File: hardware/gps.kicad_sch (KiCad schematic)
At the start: 13 parts, among them U4 L96-M33

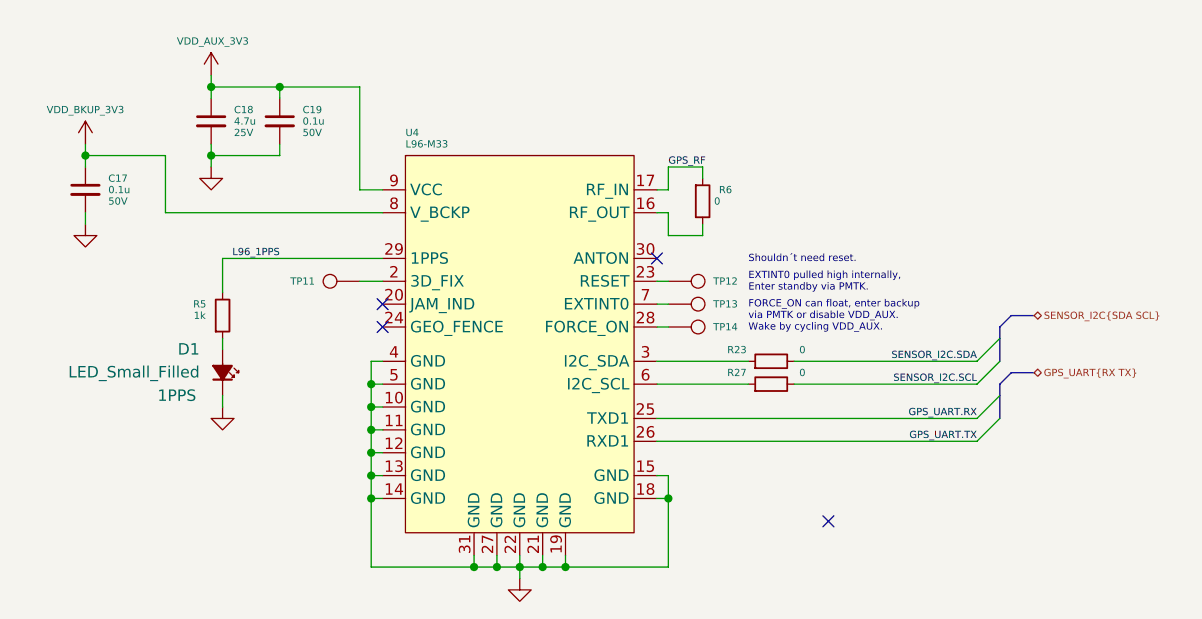
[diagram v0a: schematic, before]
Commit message: schematic tidy up, component placement, shielding investigation
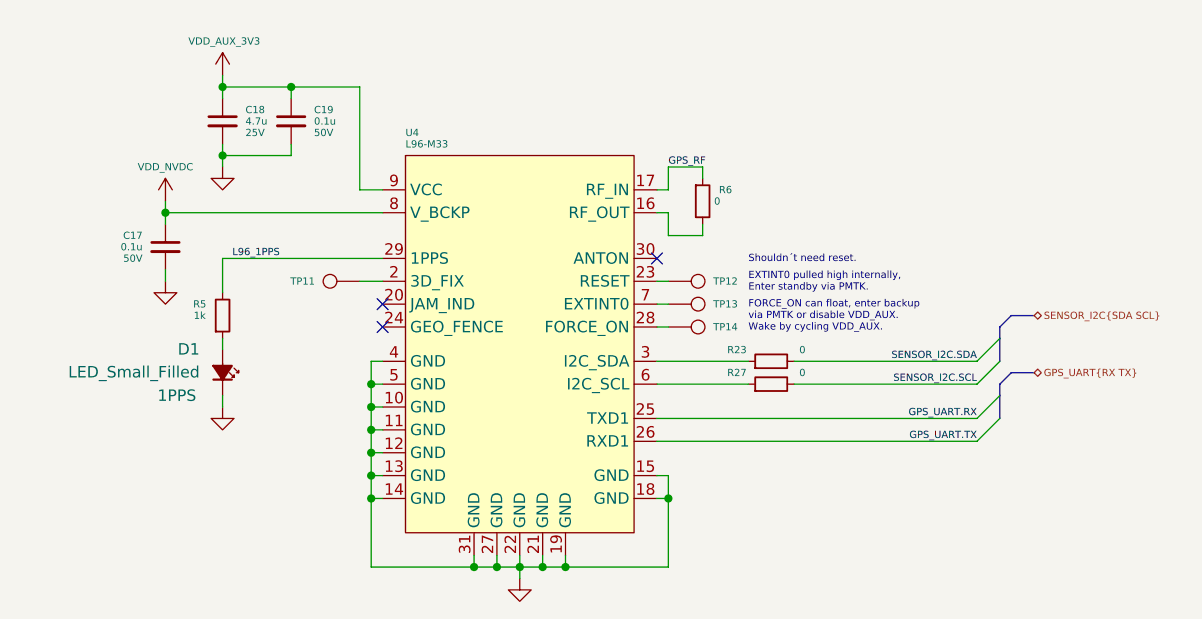
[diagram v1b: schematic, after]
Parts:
- TP12: value GPS_3DF -> GPS_RST
- TP13: value GPS_3DF -> GPS_INT
- TP14: value GPS_3DF -> GPS_FON
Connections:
- net VCC_BKUP_3V3 renamed VDD_NVDC
- no-connect marks 4 -> 3
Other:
- moved on the sheet: C17, C18, C19

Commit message: minor sch tweaks, more layout, added power emc shield
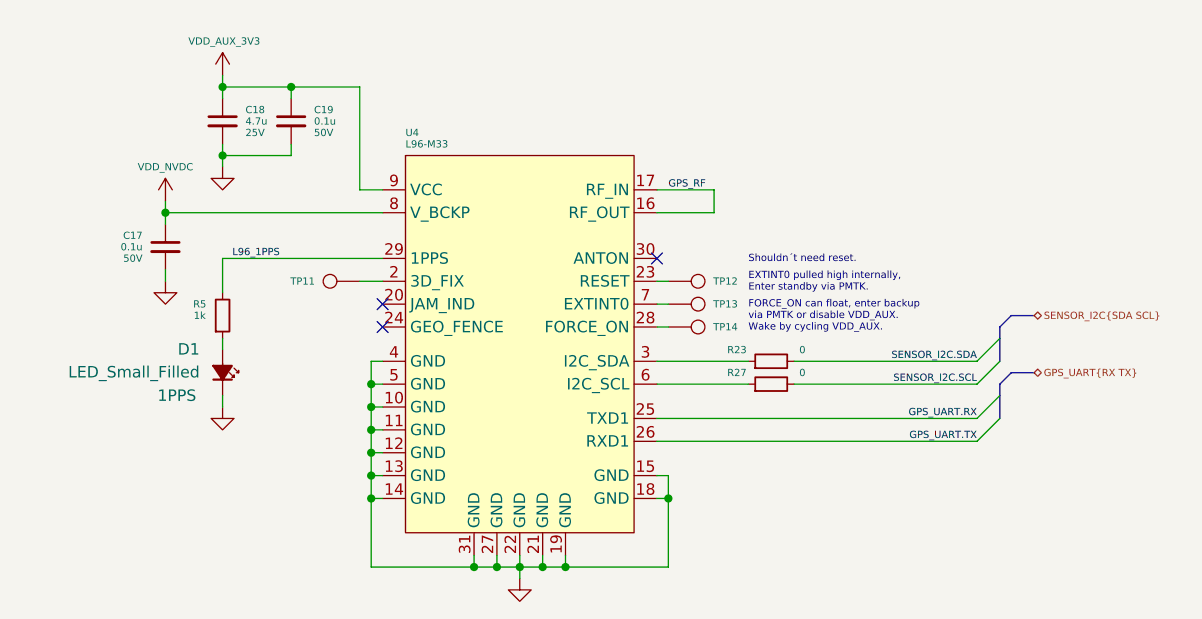
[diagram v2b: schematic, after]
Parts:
- removed R6: 0, Resistor_SMD:R_0402_1005Metric, symbol Device:R_Small
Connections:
- net GPS_RF: now also U4.16 (RF_OUT)
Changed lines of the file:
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@@
-    (stroke (width 0) (type default) (color 0 0 0 0))
-  )
-  (wire (pts (xy 168.91 85.09) (xy 172.72 85.09))
     (stroke (width 0) (type default) (color 0 0 0 0))
   )
@@
     (stroke (width 0) (type default) (color 0 0 0 0))
   )
-  (wire (pts (xy 172.72 85.09) (xy 172.72 83.82))
-    (stroke (width 0) (type default) (color 0 0 0 0))
-  )
   (wire (pts (xy 135.89 109.22) (xy 135.89 111.76))
     (stroke (width 0) (type default) (color 0 0 0 0))
@@
     (stroke (width 0) (type default) (color 0 0 0 0))
   )
-  (wire (pts (xy 168.91 80.01) (xy 168.91 77.47))
-    (stroke (width 0) (type default) (color 0 0 0 0))
-  )
   (wire (pts (xy 127 69.85) (xy 127 68.58))
     (stroke (width 0) (type default) (color 0 0 0 0))
@@
     (stroke (width 0) (type default) (color 0 0 0 0))
   )
-  (wire (pts (xy 167.64 80.01) (xy 168.91 80.01))
+  (wire (pts (xy 167.64 80.01) (xy 173.99 80.01))
     (stroke (width 0) (type default) (color 0 0 0 0))
   )
@@
     (stroke (width 0) (type default) (color 0 0 0 0))
   )
-  (wire (pts (xy 168.91 77.47) (xy 172.72 77.47))
-    (stroke (width 0) (type default) (color 0 0 0 0))
-  )
   (bus (pts (xy 205.74 101.6) (xy 207.01 100.33))
     (stroke (width 0) (type default) (color 0 0 0 0))
@@
     (stroke (width 0) (type default) (color 0 0 0 0))
   )
-  (wire (pts (xy 168.91 82.55) (xy 168.91 85.09))
+  (wire (pts (xy 173.99 80.01) (xy 173.99 82.55))
     (stroke (width 0) (type default) (color 0 0 0 0))
   )
@@
     (stroke (width 0) (type default) (color 0 0 0 0))
   )
-  (wire (pts (xy 167.64 82.55) (xy 168.91 82.55))
+  (wire (pts (xy 167.64 82.55) (xy 173.99 82.55))
     (stroke (width 0) (type default) (color 0 0 0 0))
   )
@@
   )
   (bus (pts (xy 205.74 95.25) (xy 205.74 96.52))
-    (stroke (width 0) (type default) (color 0 0 0 0))
-  )
-  (wire (pts (xy 172.72 77.47) (xy 172.72 78.74))
     (stroke (width 0) (type default) (color 0 0 0 0))
   )
@@
     (effects (font (size 0.8 0.8)) (justify right bottom))
   )
-  (label "GPS_RF" (at 168.91 77.47 0)
+  (label "GPS_RF" (at 168.91 80.01 0)
     (effects (font (size 0.8 0.8)) (justify left bottom))
   )
@@
     )
     (pin "1")
-    (pin "2")
-  )
-  (symbol (lib_id "Device:R_Small") (at 172.72 81.28 0) (unit 1)
-    (in_bom yes) (on_board yes)
-    (property "Reference" "R6" (id 0) (at 175.26 80.01 0)
-      (effects (font (size 0.8 0.8)))
-    )
-    (property "Value" "0" (id 1) (at 173.99 81.28 0)
-      (effects (font (size 0.8 0.8)) (justify left))
-    )
-    (property "Footprint" "Resistor_SMD:R_0402_1005Metric" (id 2) (at 172.72 81.28 0)
-      (effects (font (size 0.8 0.8)) hide)
-    )
-    (property "Datasheet" "~" (id 3) (at 172.72 81.28 0)
-      (effects (font (size 0.8 0.8)) hide)
-    )
-    (pin "1")

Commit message: screen mock, tweaked layout easier powerplane division
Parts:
- TP11: footprint (none) -> NetTie:NetTie-2_THT_Pad0.3mm
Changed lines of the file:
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@@
       (effects (font (size 1.27 1.27)) hide)
     )
-    (property "Footprint" "" (id 2) (at 134.62 85.09 0)
+    (property "Footprint" "NetTie:NetTie-2_THT_Pad0.3mm" (id 2) (at 134.62 85.09 0)
       (effects (font (size 1.27 1.27)) hide)
     )

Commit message: Updates
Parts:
- D1: footprint LED_SMD:LED_0603_1608Metric -> LED_SMD:LED_0402_1005Metric
- TP11: footprint NetTie:NetTie-2_THT_Pad0.3mm -> (none)
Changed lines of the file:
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@@
       (effects (font (size 1.27 1.27)) (justify right))
     )
-    (property "Footprint" "LED_SMD:LED_0603_1608Metric" (id 2) (at 119.38 100.33 90)
+    (property "Footprint" "LED_SMD:LED_0402_1005Metric" (id 2) (at 119.38 100.33 90)
       (effects (font (size 1.27 1.27)) hide)
     )
@@
       (effects (font (size 1.27 1.27)) hide)
     )
-    (property "Footprint" "NetTie:NetTie-2_THT_Pad0.3mm" (id 2) (at 134.62 85.09 0)
+    (property "Footprint" "" (id 2) (at 134.62 85.09 0)
       (effects (font (size 1.27 1.27)) hide)
     )

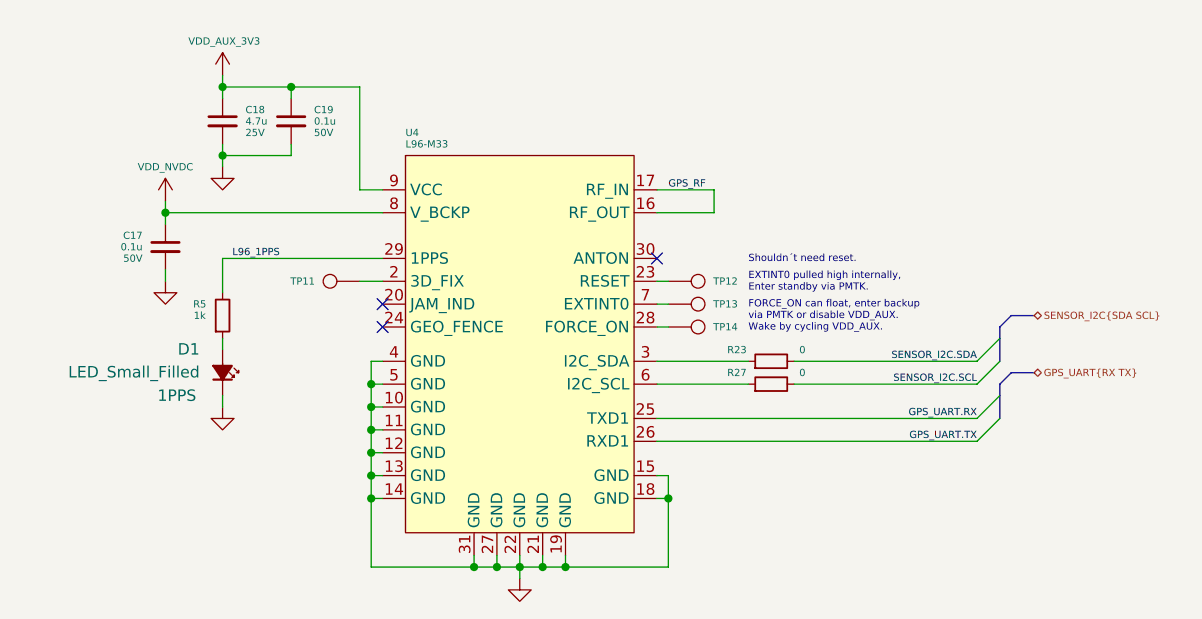
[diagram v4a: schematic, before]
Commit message: layout 0 unconnected
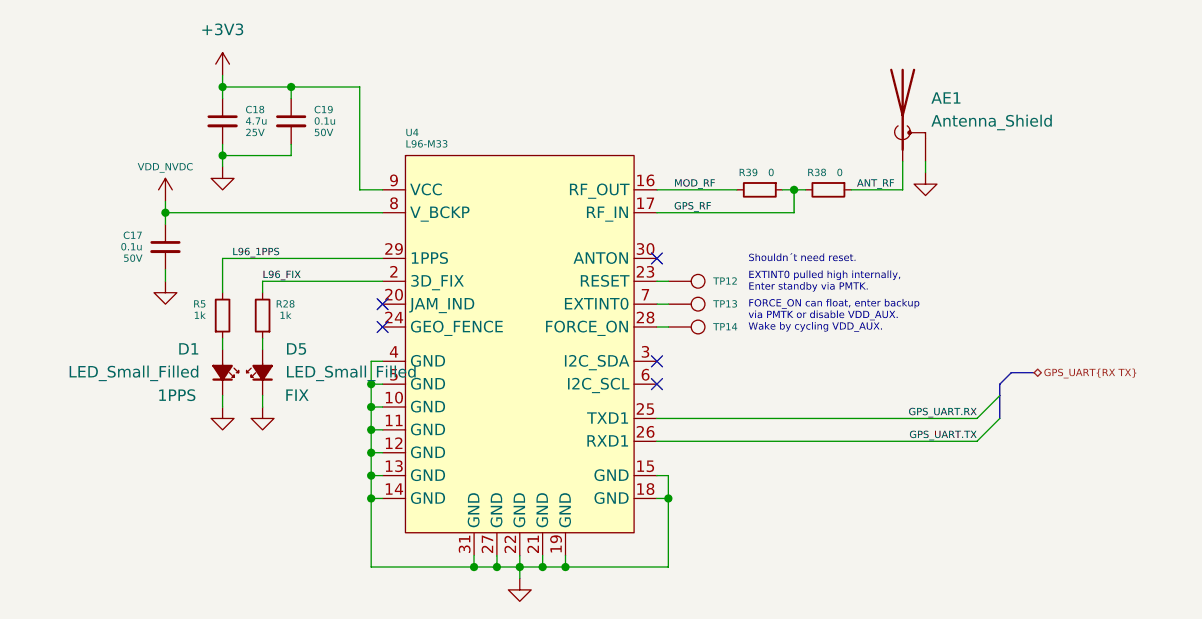
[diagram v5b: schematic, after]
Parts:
- removed R23, R27: 0, Resistor_SMD:R_0402_1005Metric, symbol Device:R_Small
- removed TP11: GPS_3DF, symbol Connector:TestPoint
- added AE1: Antenna_Shield, Connector_Coaxial:U.FL_Hirose_U.FL-R-SMT-1_Vertical, symbol Device:Antenna_Shield
- added D5: LED_Small_Filled, LED_SMD:LED_0402_1005Metric, symbol Device:LED_Small_Filled
- added R28: 1k, Resistor_SMD:R_0402_1005Metric, symbol Device:R_Small
- added R38, R39: 0, Resistor_SMD:R_0402_1005Metric, symbol Device:R_Small
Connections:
- net GND: now also AE1.2 (Shield), D5.1 (K)
- net GPS_RF: now also R38.2, R39.1; no longer U4.16 (RF_OUT)
- net L96_FIX: now reaches U4.2 (3D_FIX)
- net L96_FIX: now also R28.2
- net VDD_AUX_3V3 renamed +3V3
- new net: D5.2 (A), R28.1
- new net ANT_RF: AE1.1 (A), R38.1
- new net MOD_RF: R39.2, U4.16 (RF_OUT)
- no-connect marks 3 -> 5
